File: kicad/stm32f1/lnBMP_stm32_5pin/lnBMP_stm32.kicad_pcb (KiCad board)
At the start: 2 copper layers, 52.6 x 33 mm, 43 parts, among them J1 Debug port, J3 Debug port, J4 USB_OTG, J5 Conn_ARM_JTAG_SWD_10, U1 STM32F103CBTx, U2 LM1117-3.3, Y1 Crystal, x2 PinSocket_1x03_P1.00mm_Vertic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

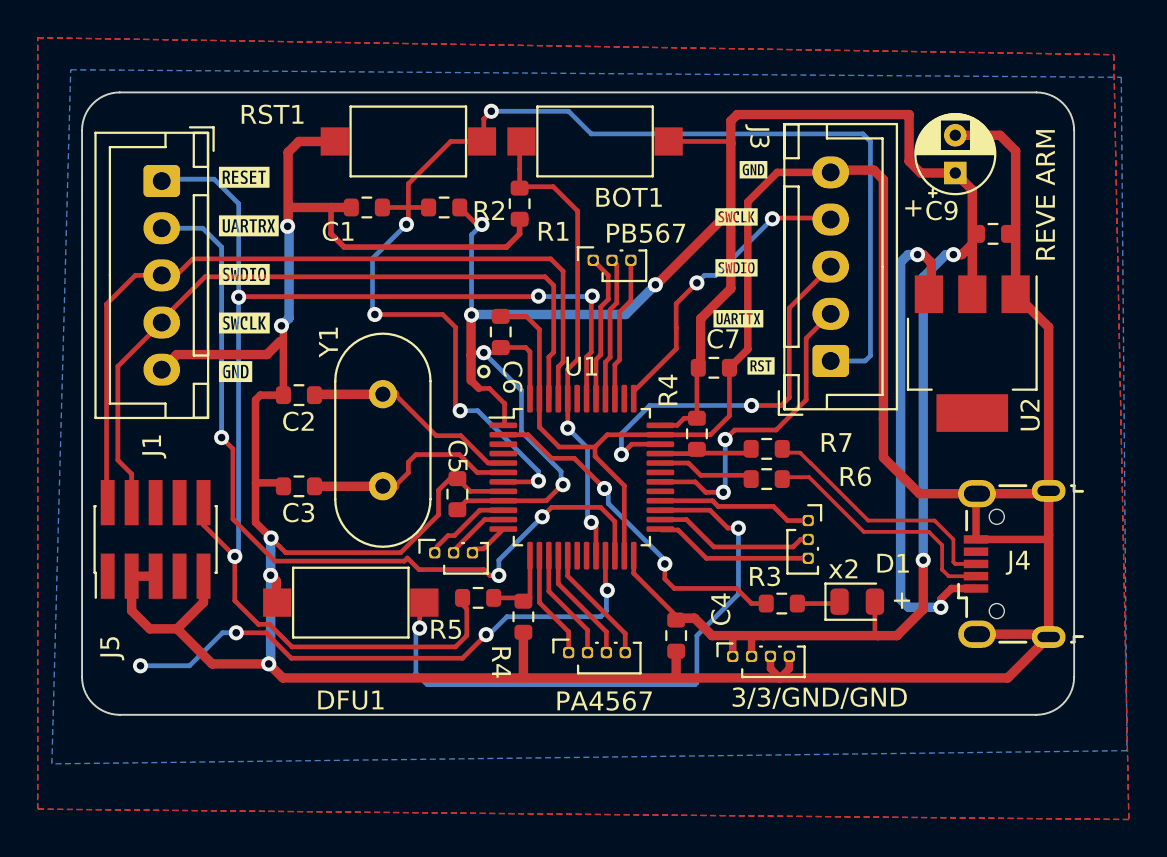
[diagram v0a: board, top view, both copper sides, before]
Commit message: kicad : switch to usbC also for stm32/gd32 boards (WIP)
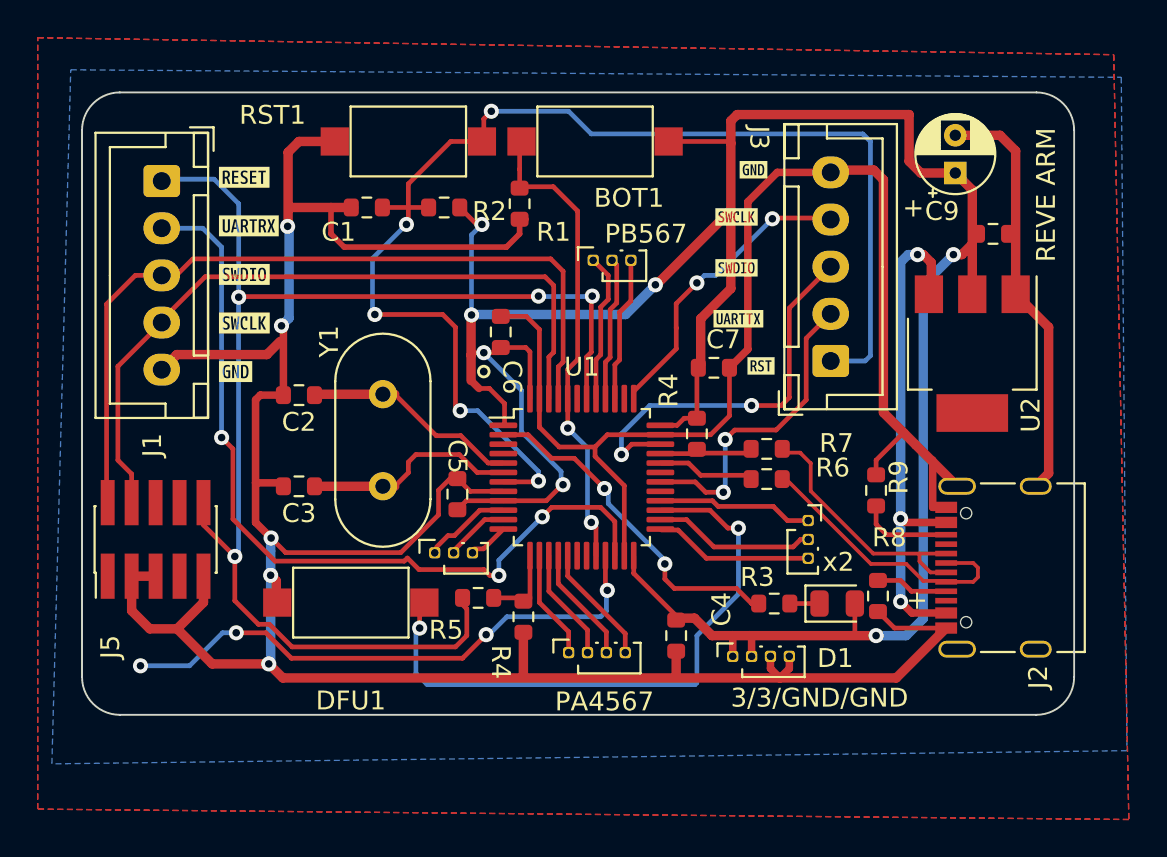
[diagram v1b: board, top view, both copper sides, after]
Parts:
- removed J4: USB_OTG, Connector_USB:USB_Micro-B_Wuerth_629105150521
- added J2: USB_C_Receptacle, Connector_USB:USB_C_Receptacle_Palconn_UTC16-G, F.Cu at (151.1, 92.2)
- added R8: 5.1k, Resistor_SMD:R_0603_1608Metric, F.Cu at (145.0, 93.7)
- added R9: 5.1k, Resistor_SMD:R_0603_1608Metric, F.Cu at (144.9, 88.1)
- moved D1 1.07 mm to (142.8, 94.1)
- moved R3 0.40 mm to (139.5, 94.1)
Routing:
- net GND: track 244.9 -> 225.8 mm
- net Net-(J2-CC2): track 0.00 -> 4.92 mm
- net Net-(J2-CC1): track 0.00 -> 3.85 mm
- net D-: track 13.1 -> 15.0 mm
- net Net-(D1-K): track 2.14 -> 1.58 mm
- net Net-(U2-VI): track 26.2 -> 26.7 mm, vias 2 -> 3

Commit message: kicad : update stm32F1 pcb
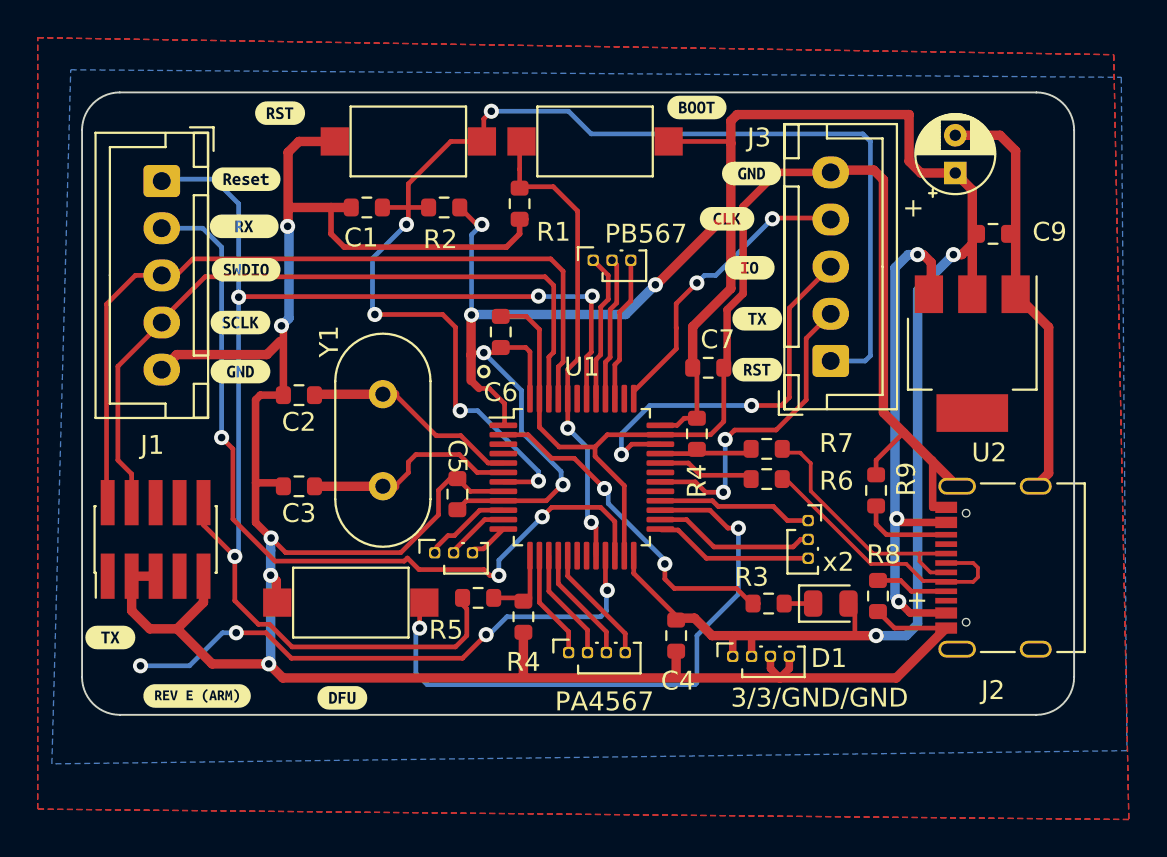
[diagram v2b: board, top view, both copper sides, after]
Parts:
- removed kibuzzard-653E87CC: G***, kibuzzard-653E87CC
- removed kibuzzard-653E87D6: G***, kibuzzard-653E87D6
- removed kibuzzard-653E87DC: G***, kibuzzard-653E87DC
- removed kibuzzard-653E87E2: G***, kibuzzard-653E87E2
- removed kibuzzard-653E87F3: G***, kibuzzard-653E87F3
- removed kibuzzard-653E8819: G***, kibuzzard-653E8819
- removed kibuzzard-653E881F: G***, kibuzzard-653E881F
- removed kibuzzard-653E8824: G***, kibuzzard-653E8824
- removed kibuzzard-653E8829: G***, kibuzzard-653E8829
- removed kibuzzard-653E882F: G***, kibuzzard-653E882F
- added kibuzzard-65C1CD6C: G***, kibuzzard-65C1CD6C, F.Cu at (111.5, 71.6)
- added kibuzzard-65C1CD89: G***, kibuzzard-65C1CD89, F.Cu at (111.4, 74.1)
- added kibuzzard-65C1CDA5: G***, kibuzzard-65C1CDA5, F.Cu at (111.5, 76.4)
- added kibuzzard-65C1CDC7: G***, kibuzzard-65C1CDC7, F.Cu at (111.2, 79.2)
- added kibuzzard-65C1CDD4: G***, kibuzzard-65C1CDD4, F.Cu at (111.2, 81.8)
- added kibuzzard-65C1CE67: G***, kibuzzard-65C1CE67, F.Cu at (108.9, 99.0)
- added kibuzzard-65C1CE83: G***, kibuzzard-65C1CE83, F.Cu at (116.6, 99.1)
- added kibuzzard-65C1CE91: G***, kibuzzard-65C1CE91, F.Cu at (113.3, 68.1)
- added kibuzzard-65C1CEA1: G***, kibuzzard-65C1CEA1, F.Cu at (135.4, 67.8)
- added kibuzzard-65C1CEC9: G***, kibuzzard-65C1CEC9, F.Cu at (138.3, 71.3)
- added kibuzzard-65C1CEEB: G***, kibuzzard-65C1CEEB, F.Cu at (137.0, 73.7)
- added kibuzzard-65C1CF10: G***, kibuzzard-65C1CF10, F.Cu at (138.2, 76.3)
- added kibuzzard-65C1CF22: G***, kibuzzard-65C1CF22, F.Cu at (138.6, 79.0)
- added kibuzzard-65C1CF2F: G***, kibuzzard-65C1CF2F, F.Cu at (138.6, 81.7)
- added kibuzzard-65C1D014: G***, kibuzzard-65C1D014, F.Cu at (104.3, 95.9)
- moved D1 0.34 mm to (142.5, 94.1)
- moved C7 0.30 mm to (136.0, 81.6)
- moved R3 0.30 mm to (139.2, 94.1)
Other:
- board text removed: "REVE ARM"

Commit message: kicad  : update (cosmetic)
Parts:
- removed kibuzzard-65C1CE67: G***, kibuzzard-65C1CE67
- added kibuzzard-65C28010: G***, kibuzzard-65C28010, F.Cu at (109.0, 99.1)

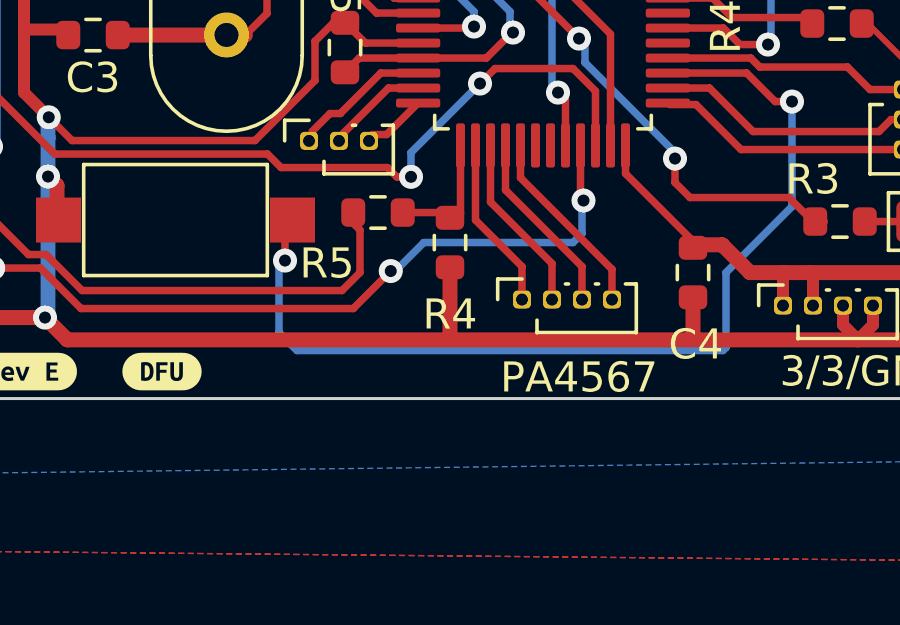
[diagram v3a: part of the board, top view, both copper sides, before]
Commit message: kicad : stm32f1 rename second r4 to rxx to avoid ambiguities
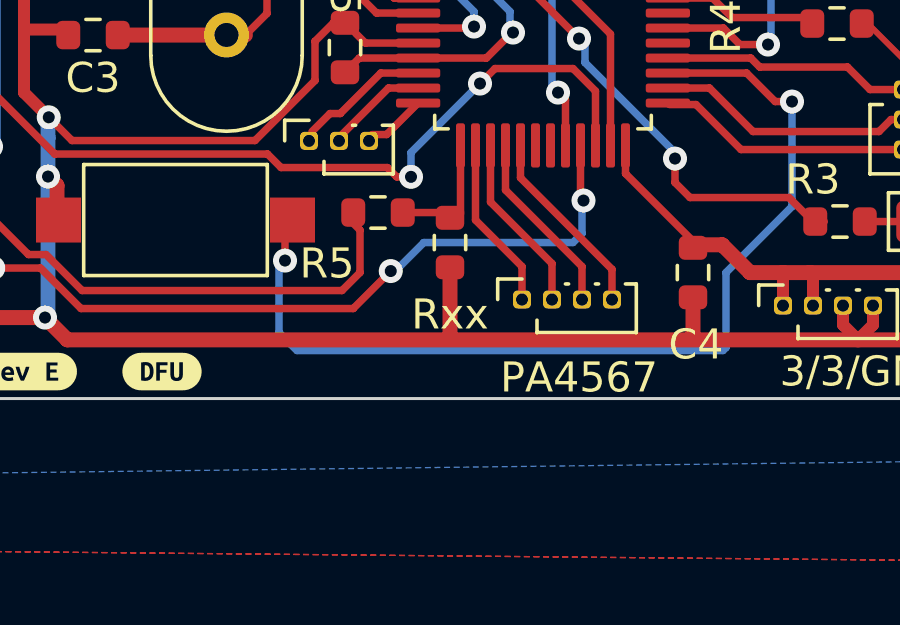
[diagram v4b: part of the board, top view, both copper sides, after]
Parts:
- renumbered R4 to Rxx
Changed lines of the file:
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@@
 (kicad_pcb
-	(version 20240108)
+	(version 20240225)
 	(generator "pcbnew")
-	(generator_version "8.0")
+	(generator_version "8.99")
 	(general
 		(thickness 1.6)
@@
 		(descr "Resistor SMD 0603 (1608 Metric), square (rectangular) end terminal, IPC_7351 nominal, (Body size source: IPC-SM-782 page 72, https://www.pcb-3d.com/wordpress/wp-content/uploads/ipc-sm-782a_amendment_1_and_2.pdf), generated with kicad-footprint-generator")
 		(tags "resistor")
-		(property "Reference" "R4"
+		(property "Reference" "Rxx"
 			(at -2.4 0 0)
 			(unlocked yes)
